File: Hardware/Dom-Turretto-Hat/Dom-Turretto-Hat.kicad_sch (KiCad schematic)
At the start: 4 parts

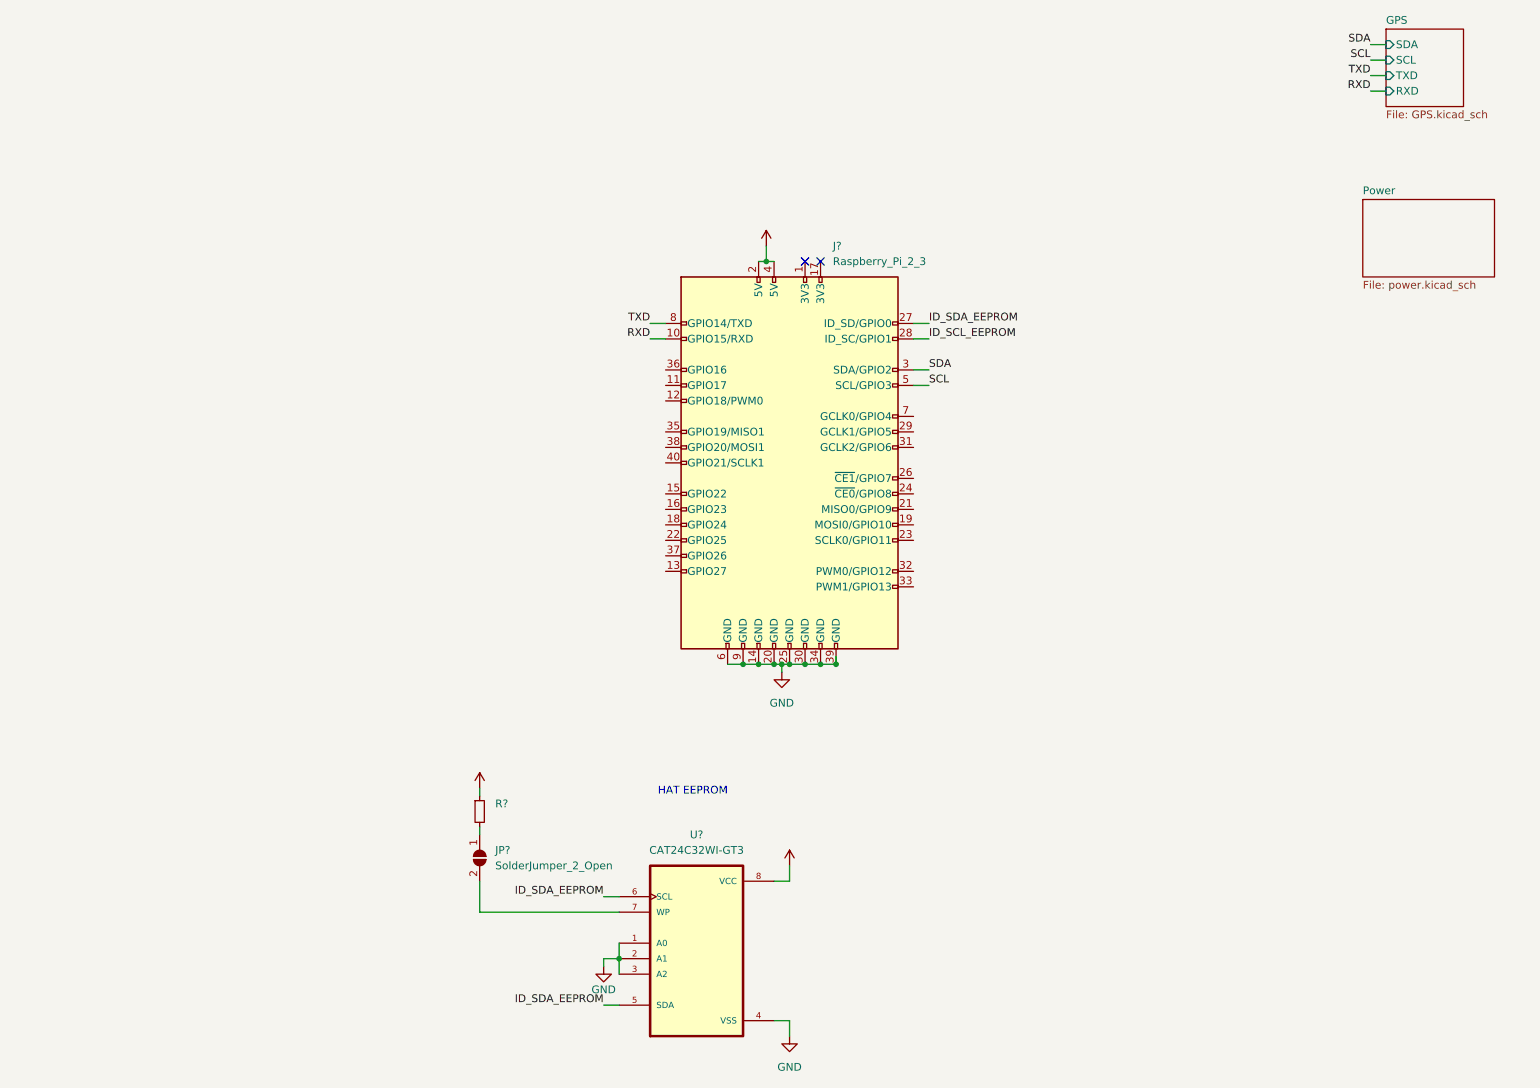
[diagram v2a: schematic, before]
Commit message: Add stepper motor drivers
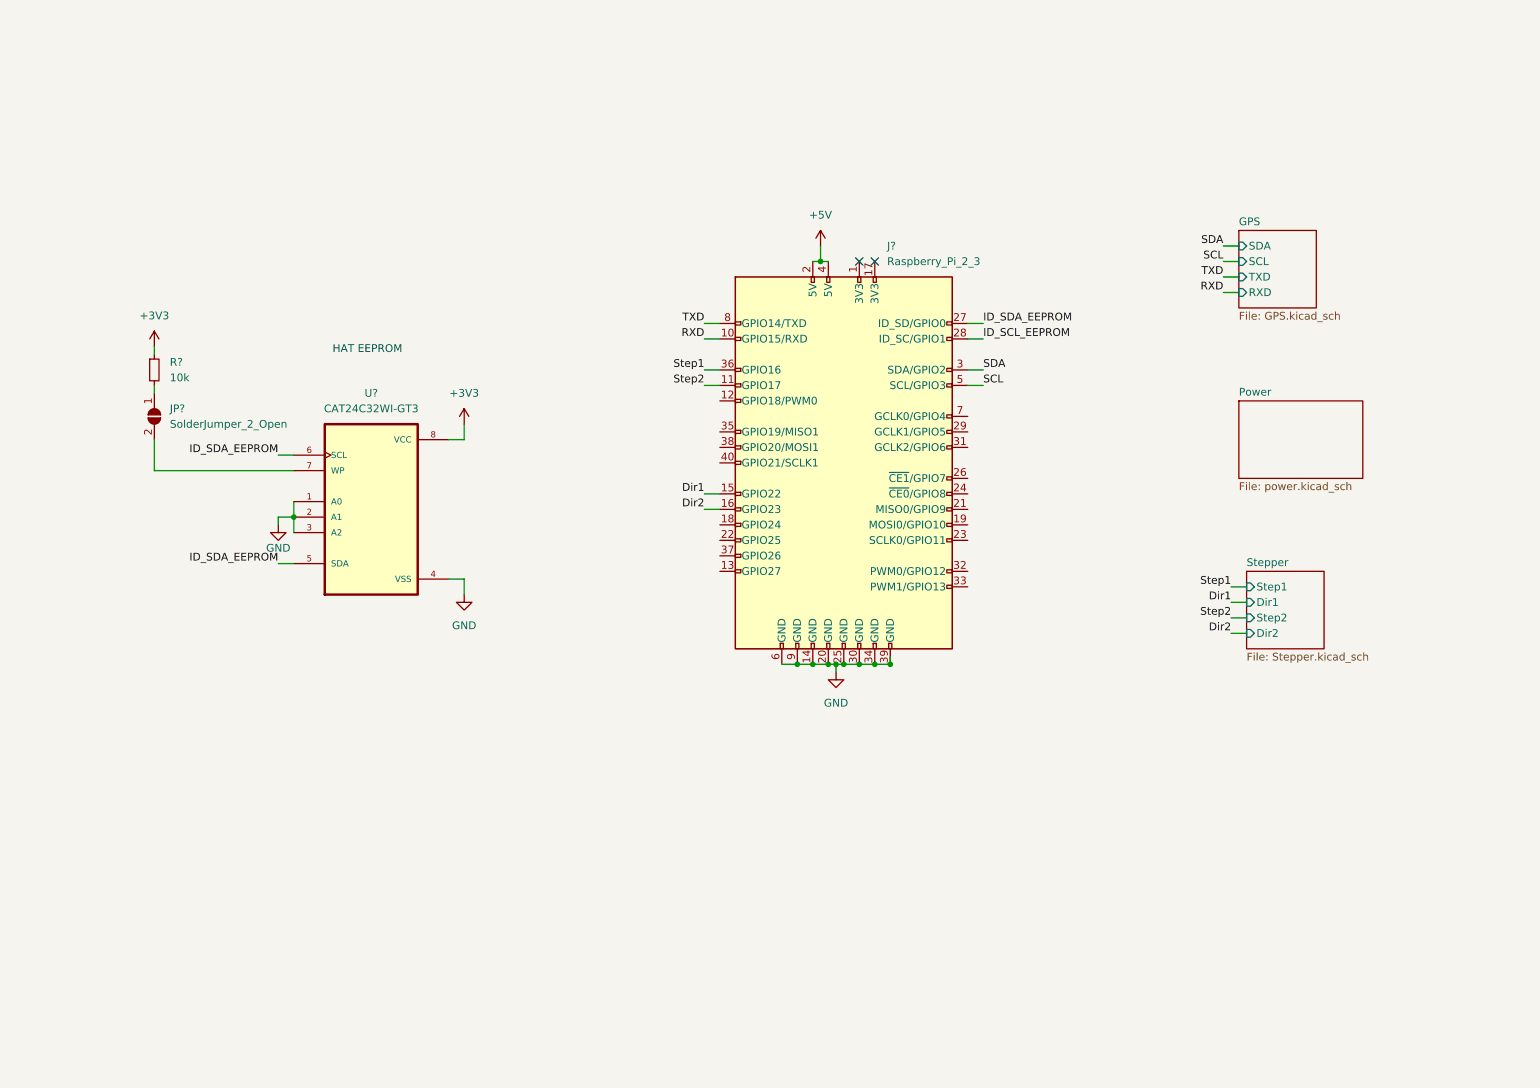
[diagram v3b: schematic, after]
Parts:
- R?: value (none) -> 10k
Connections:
- net Step2: now reaches J?.11 (GPIO17)
- net Dir1: now reaches J?.15 (GPIO22)
- net Dir2: now reaches J?.16 (GPIO23)
- net Step1: now reaches J?.36 (GPIO16)
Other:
- added sheet Stepper (Stepper.kicad_sch)
- moved on the sheet: J?, JP?, R?, U?

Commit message: Fix some stuff to make it HAT compatible
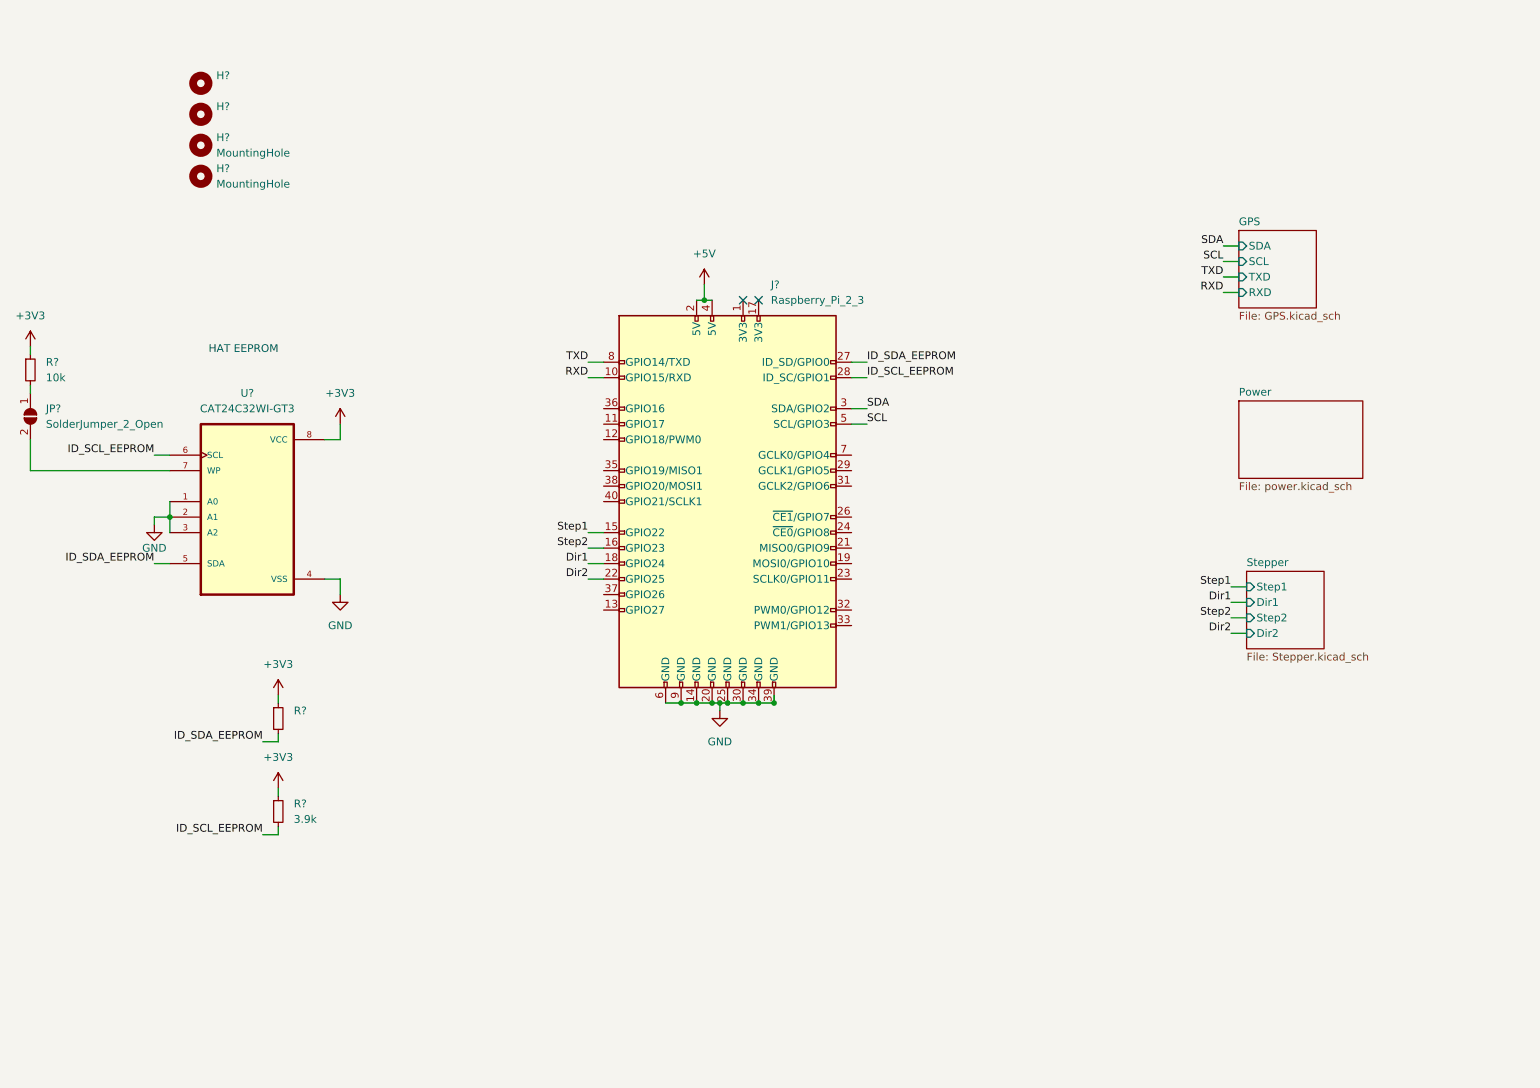
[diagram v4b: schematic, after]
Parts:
- added H? (x2): (no value), symbol Mechanical:MountingHole
- added H? (x2): MountingHole, symbol Mechanical:MountingHole
- added R?: 3.9k, symbol Device:R_Small
- added R?: (no value), symbol Device:R_Small
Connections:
- net +3V3: now also R?.1, R?.1
- net Dir1: now also J?.18 (GPIO24); no longer J?.15 (GPIO22)
- net Dir2: now also J?.22 (GPIO25); no longer J?.16 (GPIO23)
- net ID_SCL_EEPROM: now also U?.6 (SCL), R?.2
- net ID_SDA_EEPROM: now also R?.2; no longer U?.6 (SCL)
- net Step1: now also J?.15 (GPIO22); no longer J?.36 (GPIO16)
- net Step2: now also J?.16 (GPIO23); no longer J?.11 (GPIO17)
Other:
- moved on the sheet: J?, JP?, R?, U?
